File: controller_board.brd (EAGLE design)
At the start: 144 x 118 mm, 48 parts, among them J1 FRSKY-GIMBAL, J12 JST_3PIN_GND_VDD_SIG, J14 JST_3PIN_GND_VDD_SIG, J16 JST_3PIN_GND_VDD_SIG, J18 JST_3PIN_GND_VDD_SIG, J2 FRSKY-GIMBAL, J3 WIRE-HARNESS-SPARKFUN-9915, J6 HEADER-0.1IN-6POS-SCREW, J7 HEADER-0.1IN-6POS-FEMALE

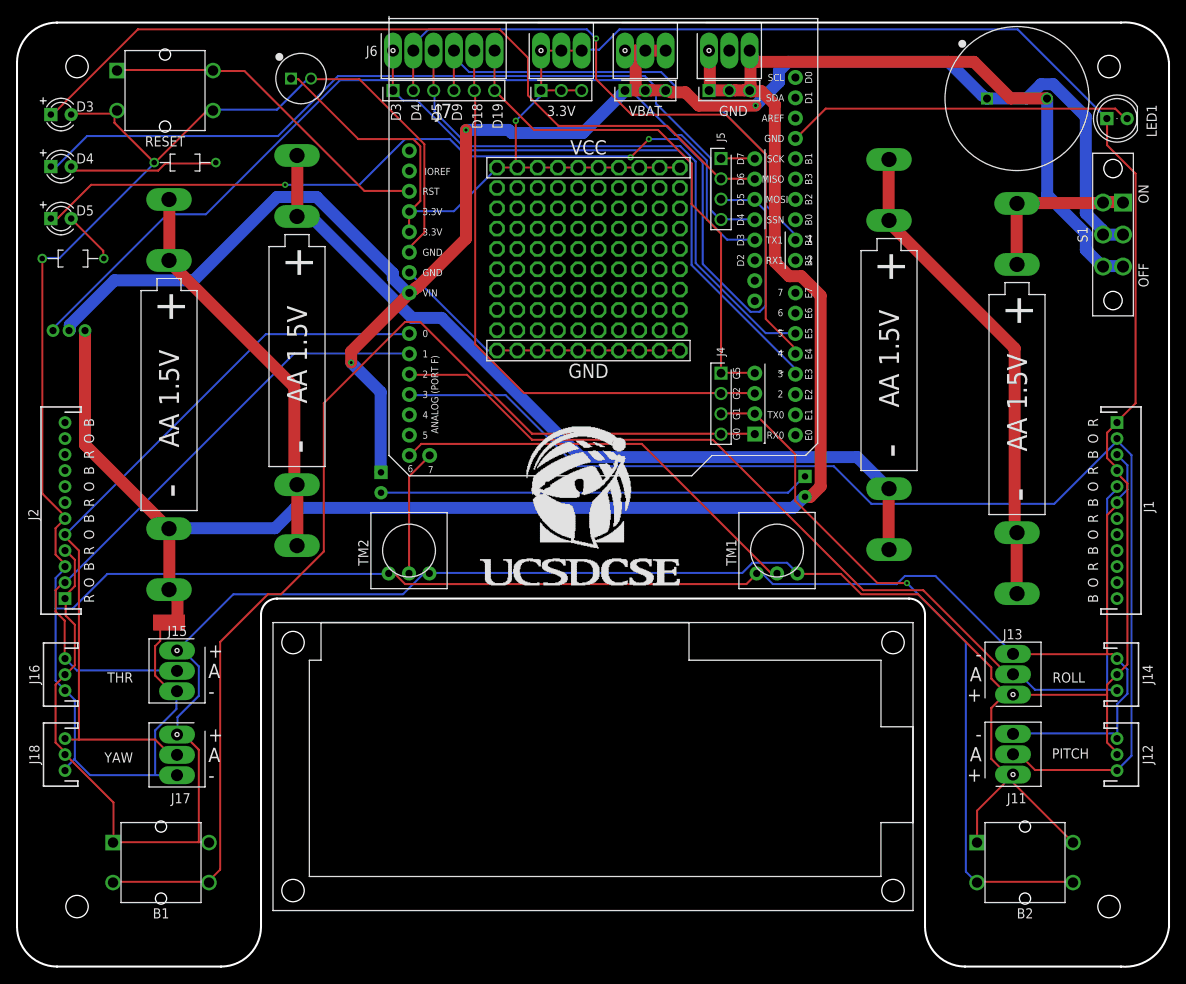
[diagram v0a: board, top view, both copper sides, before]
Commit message: Move gimbals to the underside, move leds so they are so bright an annoying
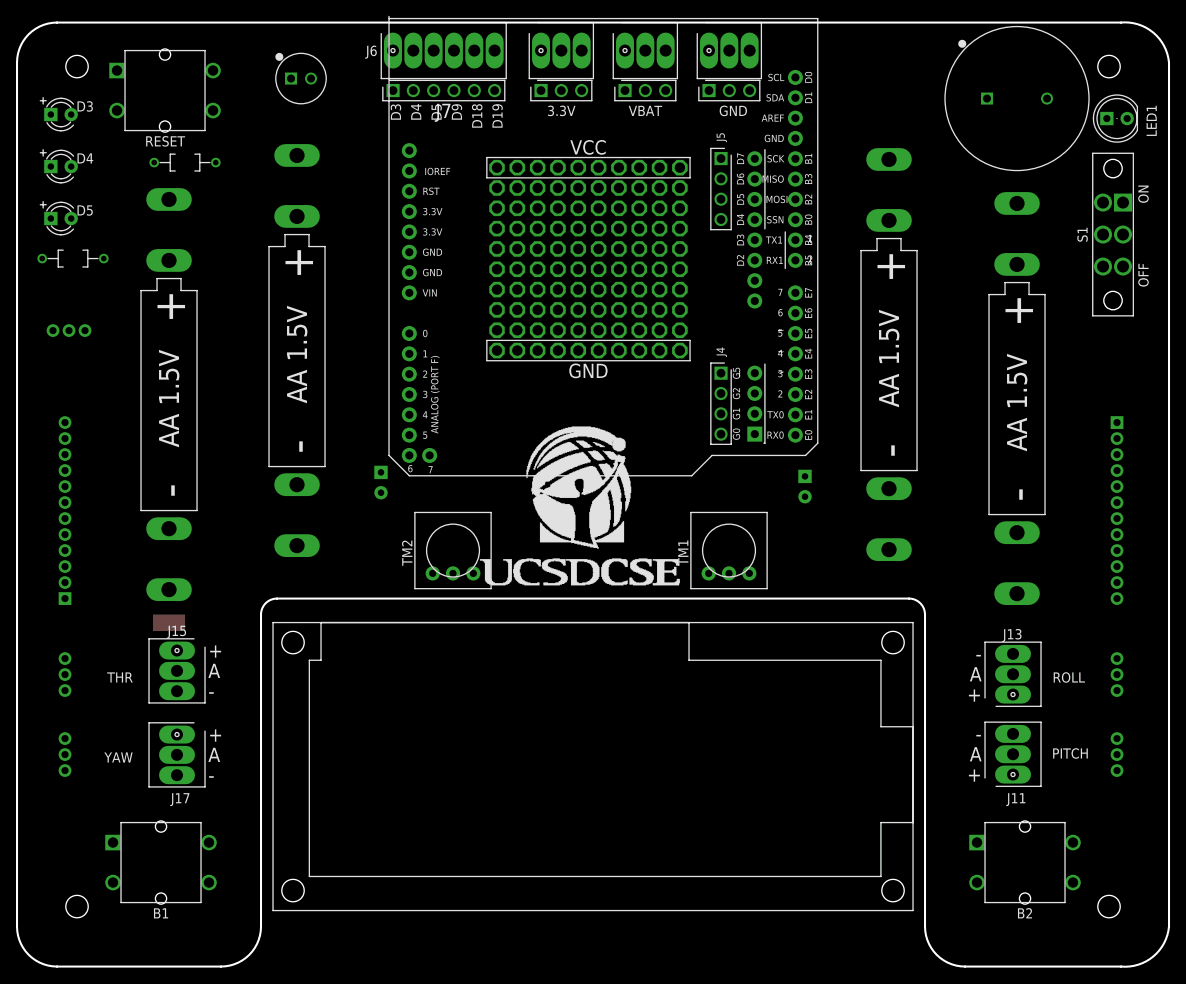
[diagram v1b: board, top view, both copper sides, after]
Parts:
- moved TM1 6.00 mm to (17.0, -8.00)
- moved TM2 5.50 mm to (-17.5, -8.00)
- flipped J1 to the bottom
- flipped J12 to the bottom
- flipped J14 to the bottom
- flipped J16 to the bottom
- flipped J18 to the bottom
- flipped J2 to the bottom
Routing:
- net +3V3: track 497.1 -> 0.00 mm, vias 1 -> 0
- net GND: track 467.1 -> 0.00 mm
- net BATGND: track 261.5 -> 0.00 mm
- net VBAT: track 221.7 -> 0.00 mm, vias 3 -> 0
- net PITCH: track 154.5 -> 0.00 mm
- net BTN1: track 142.9 -> 0.00 mm
- net ROLL: track 130.8 -> 0.00 mm
- net LED_GREEN: track 130.3 -> 0.00 mm, vias 3 -> 0
- net TX1: track 114.3 -> 0.00 mm
- net LED_RED: track 105.1 -> 0.00 mm
- net N$2: track 103.4 -> 0.00 mm
- net LED_BLUE: track 102.9 -> 0.00 mm
- net YAW: track 94.7 -> 0.00 mm
- net BTN2: track 88.7 -> 0.00 mm, vias 1 -> 0
- net D4: track 86.5 -> 0.00 mm, vias 1 -> 0
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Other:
- board text added: "Todo * check that this orientation for mirrored gimbal headers ok. * Consider moving redboard down a bit -- the parts ftdi and power jack protrude."

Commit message: Refinement based on prototype
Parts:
- moved D1 26.2 mm to (45.0, 18.5)
- moved D2 26.2 mm to (-45.0, 19.0)
- moved J3 1.12 mm to (-65.0, 20.5), turned to 0 degrees
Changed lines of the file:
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@@
 <attribute name="VALUE" x="68.7004" y="44.1966" size="1.27" layer="27" font="vector" ratio="10"/>
 </element>
-<element name="J3" library="RemotePartsB" package="WIRE-HARNESS-SPARKFUN-9915" value="WIRE-HARNESS-SPARKFUN-9915" x="-65.5" y="19.5" rot="MR180">
-<attribute name="DISTPN" value="9915" x="-65.5" y="19.5" size="1.778" layer="28" rot="MR180" display="off"/>
-<attribute name="DIST" value="Sparkfun" x="-65.5" y="19.5" size="1.778" layer="28" rot="MR180" display="off"/>
+<element name="J3" library="RemotePartsB" package="WIRE-HARNESS-SPARKFUN-9915" value="WIRE-HARNESS-SPARKFUN-9915" x="-65" y="20.5" rot="MR0">
+<attribute name="DISTPN" value="9915" x="-65" y="20.5" size="1.778" layer="28" rot="MR0" display="off"/>
+<attribute name="DIST" value="Sparkfun" x="-65" y="20.5" size="1.778" layer="28" rot="MR0" display="off"/>
 </element>
 <element name="U$3" library="Components" package="PROTO-AREA-10X10" value="PROTO-AREA-10X10" x="-12" y="17">
@@
 <attribute name="NAME" x="15.96" y="43.69" size="1.016" layer="25" font="vector" ratio="10" rot="R270" align="center"/>
 </element>
-<element name="D2" library="Components" package="LED3MM" value="" x="-26.5" y="0.5" rot="MR270">
-<attribute name="DISTPN" value="780" x="-26.5" y="0.5" size="1.778" layer="28" rot="MR270" display="off"/>
-<attribute name="DIST" value="Adafruit" x="-26.5" y="0.5" size="1.778" layer="28" rot="MR270" display="off"/>
-</element>
-<element name="D1" library="Components" package="LED3MM" value="" x="26.5" y="0" rot="MR270">
-<attribute name="DISTPN" value="780" x="26.5" y="0" size="1.778" layer="28" rot="MR270" display="off"/>
-<attribute name="DIST" value="Adafruit" x="26.5" y="0" size="1.778" layer="28" rot="MR270" display="off"/>
+<element name="D2" library="Components" package="LED3MM" value="" x="-45" y="19" rot="MR270">
+<attribute name="DISTPN" value="780" x="-45" y="19" size="1.778" layer="28" rot="MR270" display="off"/>
+<attribute name="DIST" value="Adafruit" x="-45" y="19" size="1.778" layer="28" rot="MR270" display="off"/>
+</element>
+<element name="D1" library="Components" package="LED3MM" value="" x="45" y="18.5" rot="MR270">
+<attribute name="DISTPN" value="780" x="45" y="18.5" size="1.778" layer="28" rot="MR270" display="off"/>
+<attribute name="DIST" value="Adafruit" x="45" y="18.5" size="1.778" layer="28" rot="MR270" display="off"/>
 </element>
 <element name="B2" library="Controller" package="BUTTON-TACTILE-SQUARE-ADAFRUIT1010" value="BUTTON-TACTILE-SQUARE" x="54" y="-47">
@@
 <contactref element="J3" pad="BLUE"/>
 <contactref element="U$4" pad="TX1"/>
-<wire x1="20.22" y1="30.814" x2="-67.5" y2="19.5" width="0" layer="19" extent="1-1"/>
+<wire x1="20.22" y1="30.814" x2="-63" y2="20.5" width="0" layer="19" extent="1-1"/>
 </signal>
 <signal name="N$1" class="1">
@@
 <wire x1="4" y1="54.5" x2="6.54" y2="54.5" width="0" layer="19" extent="1-1"/>
 <wire x1="-22.96" y1="24.21" x2="4" y2="49.5" width="0" layer="19" extent="1-1"/>
-<wire x1="-26.5" y1="1.77" x2="-22.96" y2="24.21" width="0" layer="19" extent="1-1"/>
-<wire x1="-65.5" y1="19.5" x2="-22.96" y2="24.21" width="0" layer="19" extent="1-1"/>
+<wire x1="-45" y1="20.27" x2="-22.96" y2="24.21" width="0" layer="19" extent="1-1"/>
+<wire x1="-65" y1="20.5" x2="-22.96" y2="24.21" width="0" layer="19" extent="1-1"/>
 </signal>
 <signal name="RESET">
@@
 <contactref element="D2" pad="K"/>
 <contactref element="D1" pad="A"/>
-<wire x1="26.5" y1="1.27" x2="-26.5" y2="-0.77" width="0" layer="19" extent="1-1"/>
+<wire x1="45" y1="19.77" x2="-45" y2="17.73" width="0" layer="19" extent="1-1"/>
 </signal>
 <signal name="BTN2">
@@
 <wire x1="19.58" y1="54.5" x2="19.58" y2="49.5" width="0" layer="19" extent="1-1"/>
 <wire x1="14.5" y1="54.5" x2="14.5" y2="49.5" width="0" layer="19" extent="1-1"/>
-<wire x1="26.5" y1="-1.27" x2="63.75" y2="27.5" width="0" layer="19" extent="1-1"/>
-<wire x1="-53" y1="-5.265" x2="26.5" y2="-1.27" width="0" layer="19" extent="1-1"/>
+<wire x1="45" y1="17.23" x2="63.75" y2="27.5" width="0" layer="19" extent="1-1"/>
+<wire x1="-53" y1="-5.265" x2="45" y2="17.23" width="0" layer="19" extent="1-1"/>
 <wire x1="-53" y1="-12.885" x2="-53" y2="-5.265" width="0" layer="19" extent="1-1"/>
 <wire x1="-52" y1="-17" x2="-53" y2="-12.885" width="0" layer="19" extent="1-1"/>
-<wire x1="-63.5" y1="19.5" x2="-53" y2="-5.265" width="0" layer="19" extent="1-1"/>
+<wire x1="-67" y1="20.5" x2="-53" y2="-5.265" width="0" layer="19" extent="1-1"/>
 </signal>
 <signal name="N$4">

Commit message: fix polarity on butons.  Connect unconnected pin on batgnd breakouts
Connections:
- net +3V3: no longer B1.P, B1.P2, B2.P, B2.P2
- net BATGND: now also GND.2
- net GND: now also B1.P, B1.P2, B2.P, B2.P2
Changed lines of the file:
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@@
 <contactref element="R4" pad="1"/>
 <contactref element="D3" pad="K"/>
+<contactref element="B1" pad="P2"/>
+<contactref element="B1" pad="P"/>
+<contactref element="B2" pad="P"/>
+<contactref element="B2" pad="P2"/>
 <wire x1="25.3" y1="43.514" x2="66.77" y2="46" width="0" layer="19" extent="1-1"/>
 <wire x1="-12" y1="17" x2="-22.96" y2="26.75" width="0" layer="19" extent="1-1"/>
@@
 <wire x1="14.46" y1="-10.8575" x2="10.86" y2="17" width="0" layer="19" extent="1-1"/>
 <wire x1="-20.04" y1="-10.8575" x2="-12" y2="17" width="0" layer="19" extent="1-1"/>
-<wire x1="-54" y1="-17" x2="-20.04" y2="-10.8575" width="0" layer="19" extent="1-1"/>
+<wire x1="-66" y1="-4" x2="-68.85" y2="28.5" width="0" layer="19" extent="1-1"/>
+<wire x1="-66" y1="-10" x2="-66" y2="-4" width="0" layer="19" extent="1-1"/>
+<wire x1="-54" y1="-17" x2="-66" y2="-10" width="0" layer="19" extent="1-1"/>
 <wire x1="-52" y1="-25.58" x2="-54" y2="-17" width="0" layer="19" extent="1-1"/>
 <wire x1="-52" y1="-36.08" x2="-52" y2="-25.58" width="0" layer="19" extent="1-1"/>
-<wire x1="-66" y1="-10" x2="-54" y2="-17" width="0" layer="19" extent="1-1"/>
-<wire x1="-66" y1="-4" x2="-66" y2="-10" width="0" layer="19" extent="1-1"/>
-<wire x1="-66" y1="-25.5" x2="-52" y2="-25.58" width="0" layer="19" extent="1-1"/>
-<wire x1="-66" y1="-35.5" x2="-66" y2="-25.5" width="0" layer="19" extent="1-1"/>
+<wire x1="-48" y1="-44.5" x2="-52" y2="-36.08" width="0" layer="19" extent="1-1"/>
+<wire x1="-60" y1="-44.5" x2="-52" y2="-36.08" width="0" layer="19" extent="1-1"/>
+<wire x1="-66" y1="-35.5" x2="-60" y2="-44.5" width="0" layer="19" extent="1-1"/>
+<wire x1="-66" y1="-25.5" x2="-66" y2="-35.5" width="0" layer="19" extent="1-1"/>
 <wire x1="52.5" y1="-20.92" x2="14.46" y2="-10.8575" width="0" layer="19" extent="1-1"/>
 <wire x1="52.5" y1="-30.92" x2="52.5" y2="-20.92" width="0" layer="19" extent="1-1"/>
 <wire x1="65.5" y1="-21.5" x2="52.5" y2="-20.92" width="0" layer="19" extent="1-1"/>
 <wire x1="65.5" y1="-31.5" x2="65.5" y2="-21.5" width="0" layer="19" extent="1-1"/>
+<wire x1="60" y1="-44.5" x2="65.5" y2="-31.5" width="0" layer="19" extent="1-1"/>
+<wire x1="48" y1="-44.5" x2="60" y2="-44.5" width="0" layer="19" extent="1-1"/>
 <wire x1="65.5" y1="-2" x2="65.5" y2="-21.5" width="0" layer="19" extent="1-1"/>
 <wire x1="65.5" y1="4" x2="65.5" y2="-2" width="0" layer="19" extent="1-1"/>
@@
 <contactref element="U$4" pad="3.3V1"/>
 <contactref element="TM2" pad="3"/>
-<contactref element="B1" pad="P2"/>
-<contactref element="B1" pad="P"/>
-<contactref element="B2" pad="P"/>
-<contactref element="B2" pad="P2"/>
 <contactref element="3.3V" pad="1"/>
 <contactref element="3.3V" pad="2"/>
@@
 <wire x1="65.5" y1="-23.5" x2="65.5" y2="2" width="0" layer="19" extent="1-1"/>
 <wire x1="65.5" y1="-33.5" x2="65.5" y2="-23.5" width="0" layer="19" extent="1-1"/>
-<wire x1="60" y1="-44.5" x2="65.5" y2="-33.5" width="0" layer="19" extent="1-1"/>
-<wire x1="52.5" y1="-36" x2="60" y2="-44.5" width="0" layer="19" extent="1-1"/>
-<wire x1="48" y1="-44.5" x2="52.5" y2="-36" width="0" layer="19" extent="1-1"/>
-<wire x1="52.5" y1="-26" x2="52.5" y2="-36" width="0" layer="19" extent="1-1"/>
+<wire x1="52.5" y1="-26" x2="65.5" y2="-23.5" width="0" layer="19" extent="1-1"/>
+<wire x1="52.5" y1="-36" x2="52.5" y2="-26" width="0" layer="19" extent="1-1"/>
 <wire x1="19.54" y1="-10.8575" x2="52.5" y2="-26" width="0" layer="19" extent="1-1"/>
 <wire x1="-14.96" y1="-10.8575" x2="19.54" y2="-10.8575" width="0" layer="19" extent="1-1"/>
 <wire x1="-52" y1="-20.5" x2="-14.96" y2="-10.8575" width="0" layer="19" extent="1-1"/>
 <wire x1="-52" y1="-31" x2="-52" y2="-20.5" width="0" layer="19" extent="1-1"/>
-<wire x1="-48" y1="-44.5" x2="-52" y2="-31" width="0" layer="19" extent="1-1"/>
-<wire x1="-60" y1="-44.5" x2="-48" y2="-44.5" width="0" layer="19" extent="1-1"/>
-<wire x1="-66" y1="-33.5" x2="-60" y2="-44.5" width="0" layer="19" extent="1-1"/>
+<wire x1="-66" y1="-33.5" x2="-52" y2="-31" width="0" layer="19" extent="1-1"/>
 <wire x1="-66" y1="-23.5" x2="-66" y2="-33.5" width="0" layer="19" extent="1-1"/>
 <wire x1="-66" y1="-14" x2="-66" y2="-23.5" width="0" layer="19" extent="1-1"/>
@@
 <contactref element="S1" pad="P$6"/>
 <contactref element="J3" pad="BLACK"/>
+<contactref element="GND" pad="2"/>
 <wire x1="63.75" y1="27.5" x2="56.75" y2="48.5" width="0" layer="19" extent="1-1"/>
 <wire x1="66.25" y1="27.5" x2="63.75" y2="27.5" width="0" layer="19" extent="1-1"/>
+<wire x1="45" y1="17.23" x2="63.75" y2="27.5" width="0" layer="19" extent="1-1"/>
 <wire x1="19.58" y1="49.5" x2="56.75" y2="48.5" width="0" layer="19" extent="1-1"/>
 <wire x1="17.04" y1="49.5" x2="19.58" y2="49.5" width="0" layer="19" extent="1-1"/>
 <wire x1="14.5" y1="49.5" x2="17.04" y2="49.5" width="0" layer="19" extent="1-1"/>
 <wire x1="19.58" y1="54.5" x2="19.58" y2="49.5" width="0" layer="19" extent="1-1"/>
-<wire x1="14.5" y1="54.5" x2="14.5" y2="49.5" width="0" layer="19" extent="1-1"/>
-<wire x1="45" y1="17.23" x2="63.75" y2="27.5" width="0" layer="19" extent="1-1"/>
-<wire x1="-53" y1="-5.265" x2="45" y2="17.23" width="0" layer="19" extent="1-1"/>
+<wire x1="17.04" y1="54.5" x2="19.58" y2="54.5" width="0" layer="19" extent="1-1"/>
+<wire x1="14.5" y1="54.5" x2="17.04" y2="54.5" width="0" layer="19" extent="1-1"/>
+<wire x1="-67" y1="20.5" x2="14.5" y2="49.5" width="0" layer="19" extent="1-1"/>
+<wire x1="-53" y1="-5.265" x2="-67" y2="20.5" width="0" layer="19" extent="1-1"/>
 <wire x1="-53" y1="-12.885" x2="-53" y2="-5.265" width="0" layer="19" extent="1-1"/>
 <wire x1="-52" y1="-17" x2="-53" y2="-12.885" width="0" layer="19" extent="1-1"/>
-<wire x1="-67" y1="20.5" x2="-53" y2="-5.265" width="0" layer="19" extent="1-1"/>
 </signal>
 <signal name="N$4">

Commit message: Connect AREF to 3.3V
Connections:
- net +3V3: now also U$4.AREF
- net BATGND: no longer S1.P$3, S1.P$6
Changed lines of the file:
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@@
 <contactref element="J18" pad="2"/>
 <contactref element="C2" pad="1"/>
+<contactref element="U$4" pad="AREF"/>
 <wire x1="65.5" y1="8" x2="64.23" y2="46" width="0" layer="19" extent="1-1"/>
 <wire x1="65.5" y1="2" x2="65.5" y2="8" width="0" layer="19" extent="1-1"/>
@@
 <wire x1="-66" y1="-14" x2="-66" y2="-23.5" width="0" layer="19" extent="1-1"/>
 <wire x1="-66" y1="-8" x2="-66" y2="-14" width="0" layer="19" extent="1-1"/>
-<wire x1="-22.96" y1="31.83" x2="-14.96" y2="-10.8575" width="0" layer="19" extent="1-1"/>
-<wire x1="-22.96" y1="34.37" x2="-22.96" y2="31.83" width="0" layer="19" extent="1-1"/>
-<wire x1="-12" y1="39.86" x2="-22.96" y2="34.37" width="0" layer="19" extent="1-1"/>
-<wire x1="-9.46" y1="39.86" x2="-12" y2="39.86" width="0" layer="19" extent="1-1"/>
-<wire x1="-6.92" y1="39.86" x2="-9.46" y2="39.86" width="0" layer="19" extent="1-1"/>
-<wire x1="-4.38" y1="39.86" x2="-6.92" y2="39.86" width="0" layer="19" extent="1-1"/>
-<wire x1="-1.84" y1="39.86" x2="-4.38" y2="39.86" width="0" layer="19" extent="1-1"/>
-<wire x1="0.7" y1="39.86" x2="-1.84" y2="39.86" width="0" layer="19" extent="1-1"/>
-<wire x1="3.24" y1="39.86" x2="0.7" y2="39.86" width="0" layer="19" extent="1-1"/>
-<wire x1="5.78" y1="39.86" x2="3.24" y2="39.86" width="0" layer="19" extent="1-1"/>
-<wire x1="8.32" y1="39.86" x2="5.78" y2="39.86" width="0" layer="19" extent="1-1"/>
-<wire x1="10.86" y1="39.86" x2="8.32" y2="39.86" width="0" layer="19" extent="1-1"/>
+<wire x1="25.3" y1="46.054" x2="64.23" y2="46" width="0" layer="19" extent="1-1"/>
+<wire x1="10.86" y1="39.86" x2="25.3" y2="46.054" width="0" layer="19" extent="1-1"/>
+<wire x1="8.32" y1="39.86" x2="10.86" y2="39.86" width="0" layer="19" extent="1-1"/>
+<wire x1="5.78" y1="39.86" x2="8.32" y2="39.86" width="0" layer="19" extent="1-1"/>
+<wire x1="3.24" y1="39.86" x2="5.78" y2="39.86" width="0" layer="19" extent="1-1"/>
+<wire x1="0.7" y1="39.86" x2="3.24" y2="39.86" width="0" layer="19" extent="1-1"/>
+<wire x1="-1.84" y1="39.86" x2="0.7" y2="39.86" width="0" layer="19" extent="1-1"/>
+<wire x1="-4.38" y1="39.86" x2="-1.84" y2="39.86" width="0" layer="19" extent="1-1"/>
+<wire x1="-6.92" y1="39.86" x2="-4.38" y2="39.86" width="0" layer="19" extent="1-1"/>
+<wire x1="-9.46" y1="39.86" x2="-6.92" y2="39.86" width="0" layer="19" extent="1-1"/>
+<wire x1="-12" y1="39.86" x2="-9.46" y2="39.86" width="0" layer="19" extent="1-1"/>
 <wire x1="-1.42" y1="49.5" x2="-1.84" y2="39.86" width="0" layer="19" extent="1-1"/>
 <wire x1="-3.96" y1="49.5" x2="-1.42" y2="49.5" width="0" layer="19" extent="1-1"/>
@@
 <wire x1="-3.96" y1="54.5" x2="-1.42" y2="54.5" width="0" layer="19" extent="1-1"/>
 <wire x1="-6.5" y1="54.5" x2="-3.96" y2="54.5" width="0" layer="19" extent="1-1"/>
+<wire x1="-22.96" y1="34.37" x2="-12" y2="39.86" width="0" layer="19" extent="1-1"/>
+<wire x1="-22.96" y1="31.83" x2="-22.96" y2="34.37" width="0" layer="19" extent="1-1"/>
 <wire x1="-37.75" y1="51" x2="-22.96" y2="34.37" width="0" layer="19" extent="1-1"/>
 </signal>
@@
 <contactref element="D1" pad="K"/>
 <contactref element="C1" pad="2"/>
-<contactref element="S1" pad="P$3"/>
-<contactref element="S1" pad="P$6"/>
 <contactref element="J3" pad="BLACK"/>
 <contactref element="GND" pad="2"/>
-<wire x1="63.75" y1="27.5" x2="56.75" y2="48.5" width="0" layer="19" extent="1-1"/>
-<wire x1="66.25" y1="27.5" x2="63.75" y2="27.5" width="0" layer="19" extent="1-1"/>
-<wire x1="45" y1="17.23" x2="63.75" y2="27.5" width="0" layer="19" extent="1-1"/>
+<wire x1="45" y1="17.23" x2="56.75" y2="48.5" width="0" layer="19" extent="1-1"/>
 <wire x1="19.58" y1="49.5" x2="56.75" y2="48.5" width="0" layer="19" extent="1-1"/>
 <wire x1="17.04" y1="49.5" x2="19.58" y2="49.5" width="0" layer="19" extent="1-1"/>
